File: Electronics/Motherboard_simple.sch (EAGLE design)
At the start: 23 parts

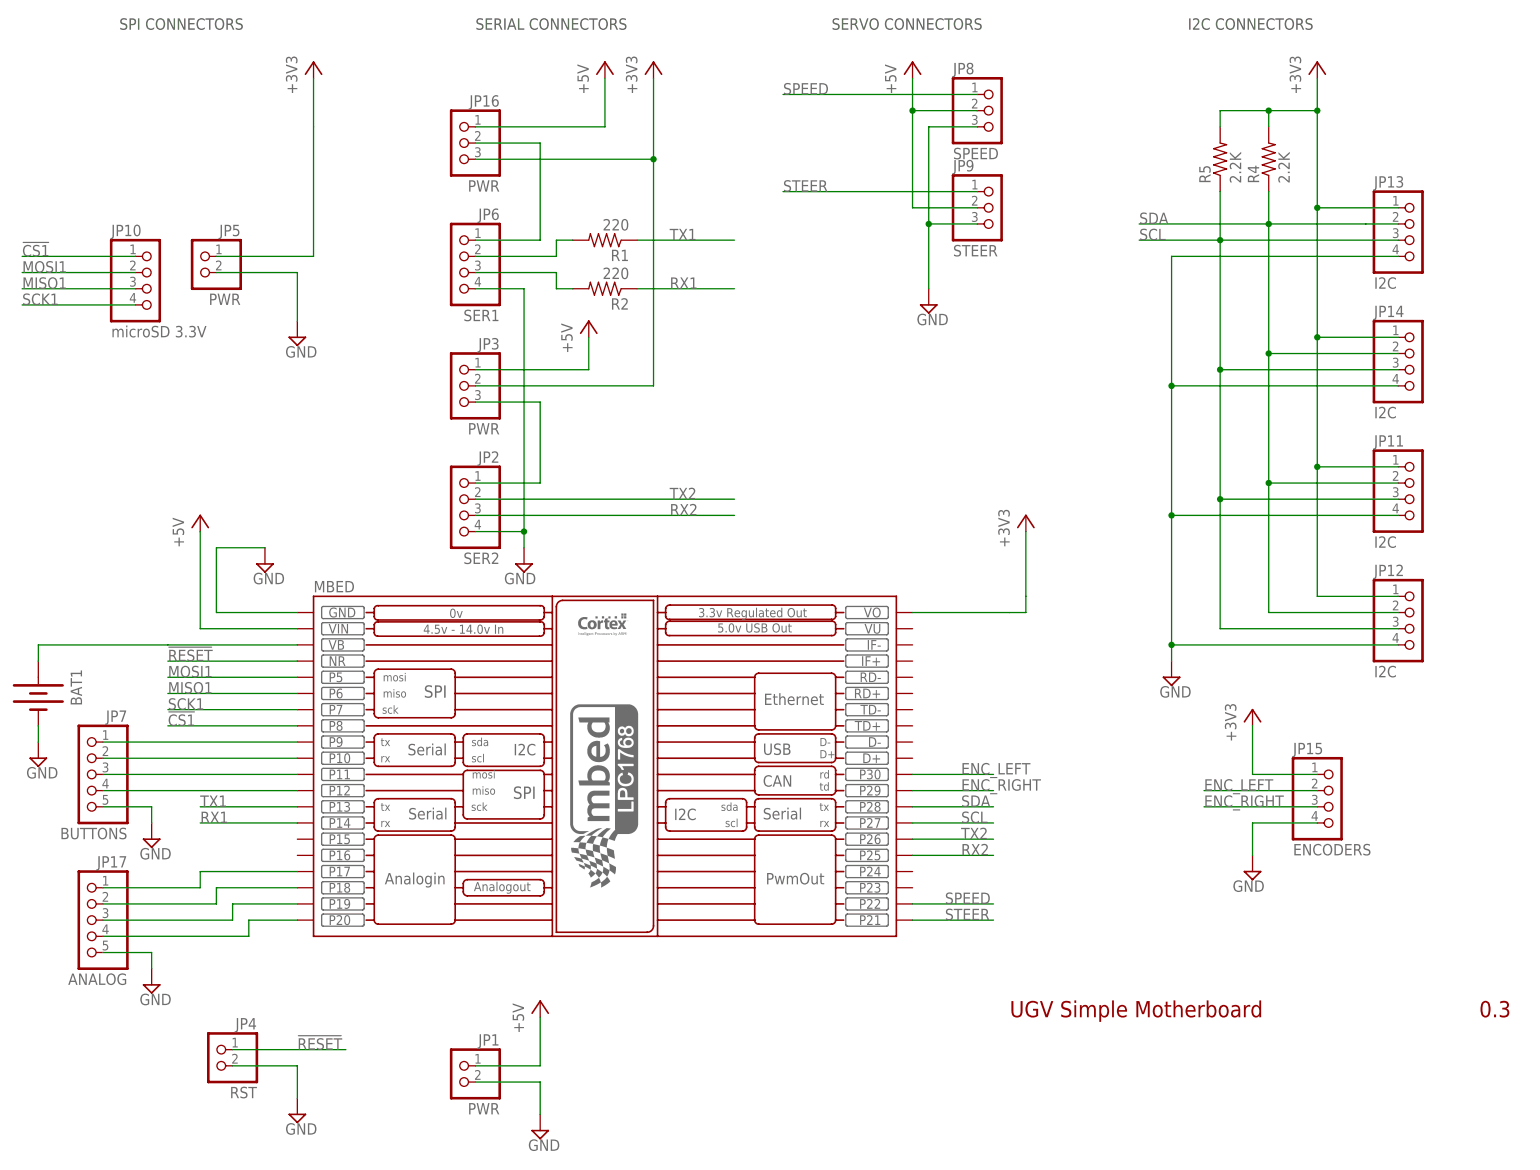
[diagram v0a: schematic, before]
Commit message: Initial Revision for microSD breakout, revised microsd pin header for motherboard, other minor tweaks to motherboard.
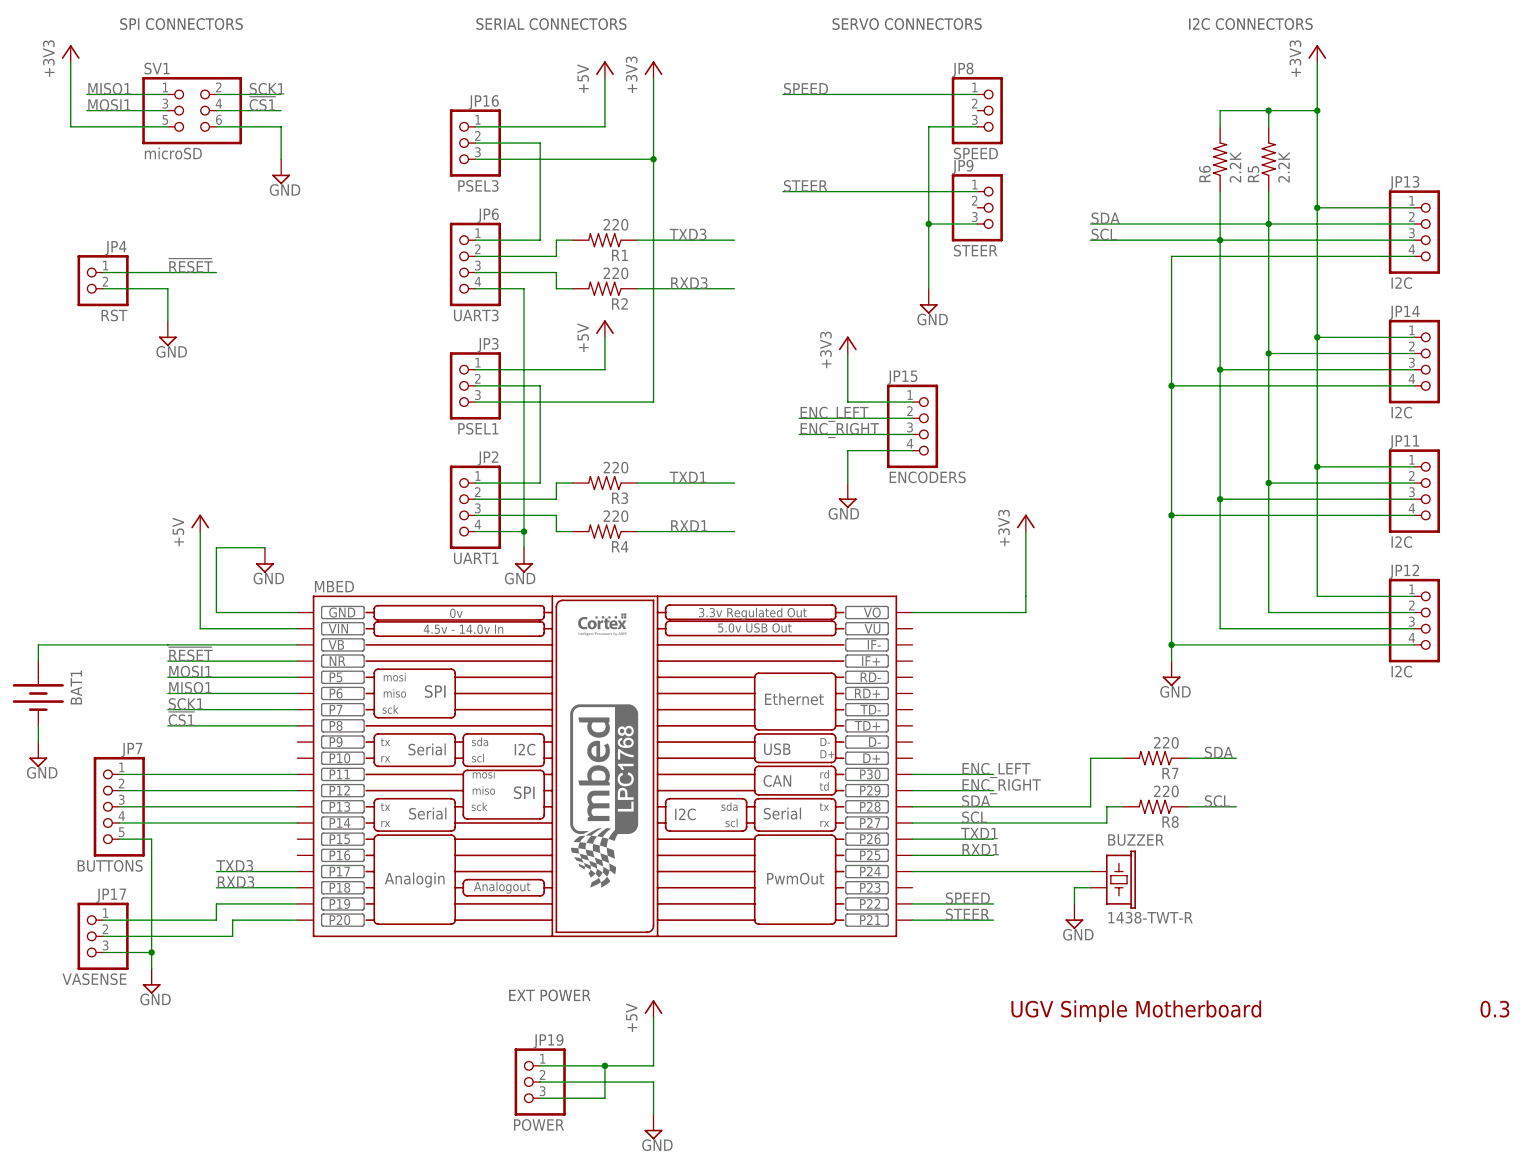
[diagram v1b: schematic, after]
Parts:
- removed JP1: PWR, pinhead-2:PINHD-1X02_2.54-90°-S
- removed JP10: microSD 3.3V, pinhead-2:PINHD-1X04_2.54-S
- removed JP5: PWR, pinhead-2:PINHD-1X02_2.54-S
- added BUZZER: 1438-TWT-R, mes_buzzers:BUZZER-AT-1438-TWT-R
- added JP19: POWER, pinhead-2:PINHD-1X03_2.54-S
- added R3, R7, R8: 220, rcl:R-US_R0805
- added R6: 2.2K, rcl:R-US_0204/5
- added SV1: microSD, pinhead-2:PINHD-2X03_2.54
- BAT1: MF (none) -> KEYSTONE ELECTR; MPN (none) -> 3001; OC_NEWARK (none) -> 66F5623; PARTNO (none) -> 3001
- JP11, JP12, JP13, JP14, JP15, JP4, JP7, JP8, JP9, R5: OC_NEWARK (none) -> unknown
- JP16: value PWR -> PSEL3; MPN (none) -> BF020-03-A-B-0600-0300-N-G; OC_NEWARK (none) -> 67R7706
- JP17: value ANALOG -> VASENSE; device pinhead-2:PINHD-1X05_2.54-S -> pinhead-2:PINHD-1X03_2.54-S; OC_NEWARK (none) -> unknown
- JP2: value SER2 -> UART1; OC_NEWARK (none) -> unknown
- JP3: value PWR -> PSEL1; MPN (none) -> BF020-03-A-B-0600-0300-N-G; OC_NEWARK (none) -> 67R7706
- JP6: value SER1 -> UART3; OC_NEWARK (none) -> unknown
- MBED: MPN (none) -> 2212S-20SG-85; OC_NEWARK (none) -> 08N6778
- R1, R2: device rcl:R-US_R0603 -> rcl:R-US_R0805; MPN (none) -> WCR0805-220RFI; OC_NEWARK (none) -> 98K2621
- R4: value 2.2K -> 220; device rcl:R-US_0204/5 -> rcl:R-US_R0805; MPN (none) -> WCR0805-220RFI; OC_NEWARK (none) -> 98K2621
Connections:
- removed net RX1: MBED.P14, R2.1
- removed net RX2: JP2.3, MBED.P25
- removed net TX1: MBED.P13, R1.1
- removed net TX2: JP2.2, MBED.P26
- new net N$12: BUZZER.1, MBED.P24
- new net N$13: MBED.P28, R7.2
- new net N$14: MBED.P27, R8.2
- new net RXD1: MBED.P25, R4.1
- new net RXD3: MBED.P18, R2.1
- new net TXD1: MBED.P26, R3.1
- new net TXD3: MBED.P17, R1.1
- net !CS1: now also SV1.4; no longer JP10.1
- net +3V3: now also JP3.3, R6.2, SV1.5; no longer JP3.2, JP5.1, R4.2
- net +5V: now also JP19.1, JP19.3; no longer JP1.1, JP8.2, JP9.2
- net AMP: now also JP17.2; no longer JP17.4
- net GND: now also BUZZER.2, JP17.3, JP19.2, SV1.6; no longer JP1.2, JP17.5, JP5.2
- net MISO1: now also SV1.1; no longer JP10.3
- net MOSI1: now also SV1.3; no longer JP10.2
- net N$10: now also JP2.3, R4.2; no longer JP17.1, MBED.P17
- net N$11: now also JP3.2; no longer JP3.3
- net N$4: now also MBED.P11; no longer MBED.P9
- net N$5: now also MBED.P12; no longer MBED.P10
- net N$6: now also JP17.1; no longer JP17.3
- net N$7: now also MBED.P13; no longer MBED.P11
- net N$8: now also MBED.P14; no longer MBED.P12
- net N$9: now also JP2.2, R3.2; no longer JP17.2, MBED.P18
- net SCK1: now also SV1.2; no longer JP10.4
- net SCL: now also R6.1, R8.1; no longer MBED.P27, R5.1
- net SDA: now also R5.1, R7.1; no longer MBED.P28, R4.1
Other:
- note added: "EXT POWER"
- moved on the sheet: JP11, JP12, JP13, JP14, JP15, JP4, JP7, R4, R5

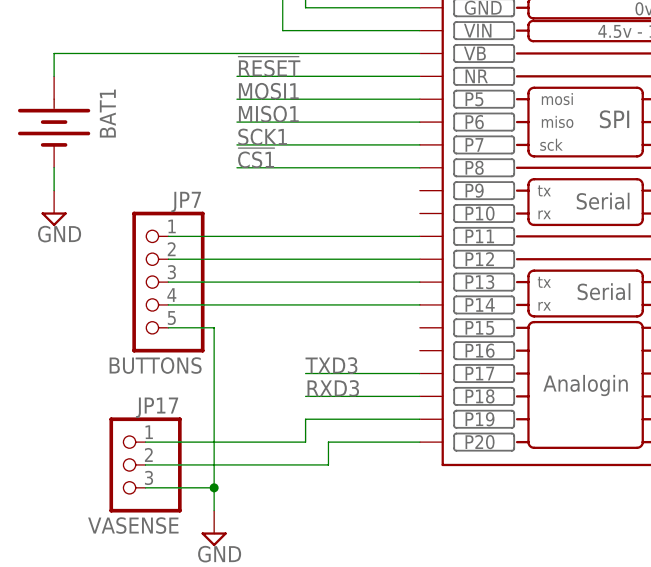
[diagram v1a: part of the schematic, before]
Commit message: Tweaks to make room for SPI2
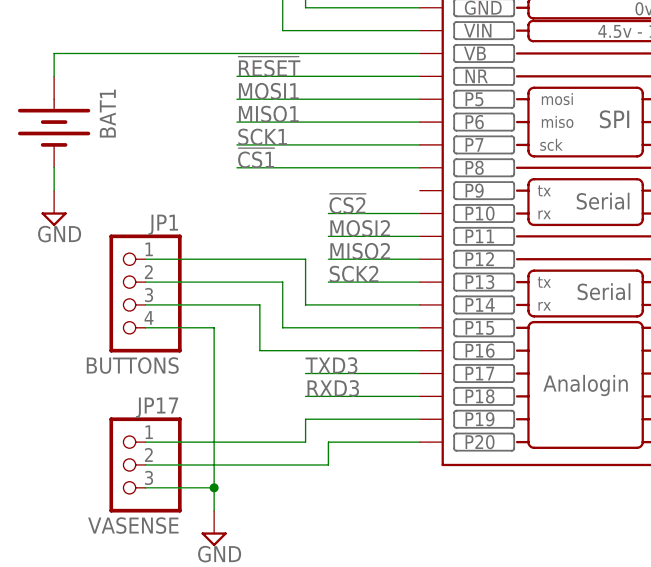
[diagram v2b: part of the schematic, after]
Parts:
- removed JP7: BUTTONS, pinhead-2:PINHD-1X05_2.54-S
- added JP1: BUTTONS, pinhead-2:PINHD-1X04_2.54-S
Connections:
- removed net N$4: JP7.1, MBED.P11
- new net !CS2: MBED.P10
- new net MISO2: MBED.P12
- new net MOSI2: MBED.P11
- new net SCK2: MBED.P13
- net GND: now also JP1.4; no longer JP7.5
- net N$5: now also JP1.1, MBED.P14; no longer JP7.2, MBED.P12
- net N$7: now also JP1.2, MBED.P15; no longer JP7.3, MBED.P13
- net N$8: now also JP1.3, MBED.P16; no longer JP7.4, MBED.P14

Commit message: Minor updates and tweaks
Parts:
- removed JP16: PSEL3, pinhead-2:PINHD-1X03_2.54-S
- removed JP3: PSEL1, pinhead-2:PINHD-1X03_2.54-S
- added JP10: UART2, pinhead-2:PINHD-1X04_2.54-S
- added JP5: I2C, pinhead-2:PINHD-1X04_2.54-S
- added JP7: PPS, pinhead-2:PINHD-1X01_2.54-S
- added R10, R9: 220, rcl:R-US_R0805
- BAT1: device SparkFun:BATTERY12PTH -> SparkFun:BATTERY12MM
- JP1: device pinhead-2:PINHD-1X04_2.54-S -> pinhead-2:PINHD-2X02_2.54; OC_NEWARK unknown -> (none)
- JP17: value VASENSE -> VA
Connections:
- removed net !CS2: MBED.P10
- removed net MISO2: MBED.P12
- removed net MOSI2: MBED.P11
- removed net N$11: JP2.1, JP3.2
- removed net N$3: JP16.2, JP6.1
- removed net SCK2: MBED.P13
- new net N$16: JP10.2, R9.2
- new net N$17: JP10.3, R10.2
- new net PPS: JP7.1, MBED.P23
- new net RXD2: MBED.P10, R10.1
- new net TXD2: MBED.P9, R9.1
- net +3V3: now also JP10.1, JP2.1, JP5.1, JP6.1; no longer JP16.3, JP3.3
- net +5V: no longer JP16.1, JP3.1
- net GND: now also JP1.1, JP10.4, JP5.4; no longer JP1.4
- net N$5: now also JP1.2; no longer JP1.1
- net N$7: now also JP1.4; no longer JP1.2
- net SCL: now also JP5.3
- net SDA: now also JP5.2
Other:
- moved on the sheet: JP1, JP11, JP12, JP13, JP14, JP17, JP2, JP4, JP6, R1, R2, R3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

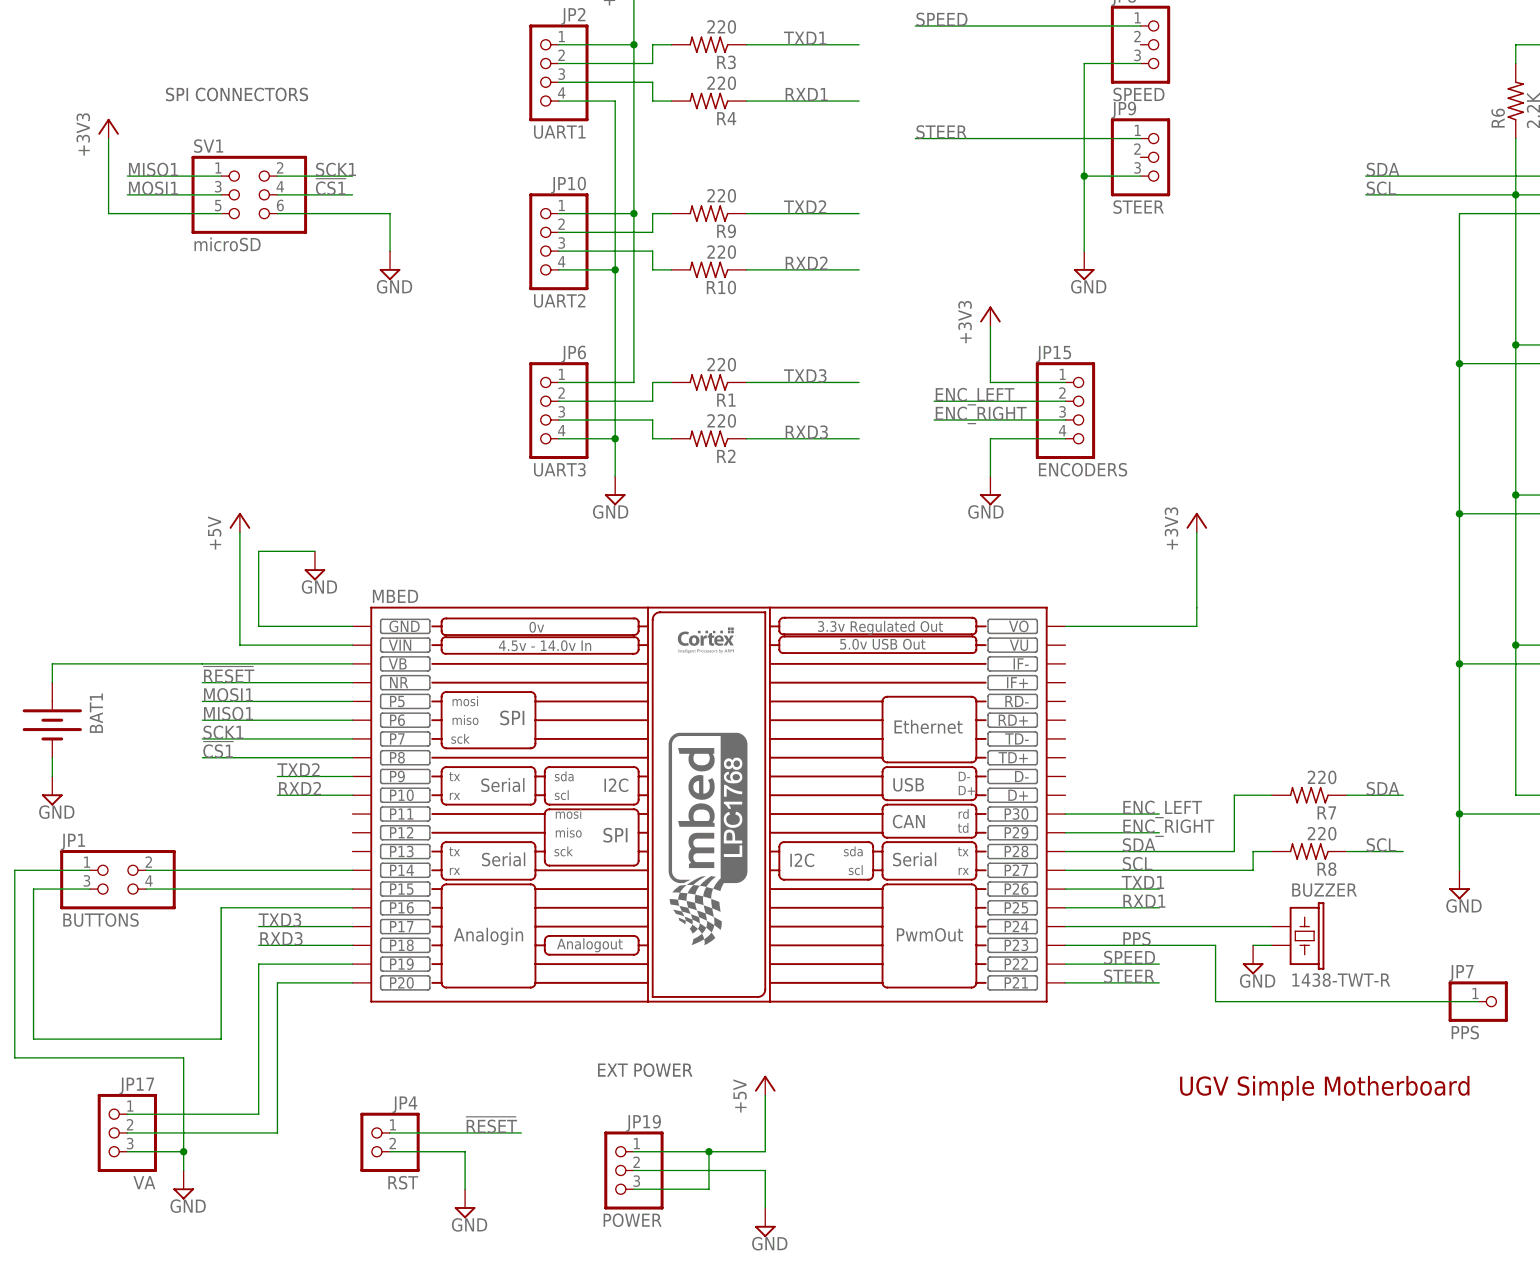
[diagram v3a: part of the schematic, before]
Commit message: Removed battery, added microSD, more room now, yay.
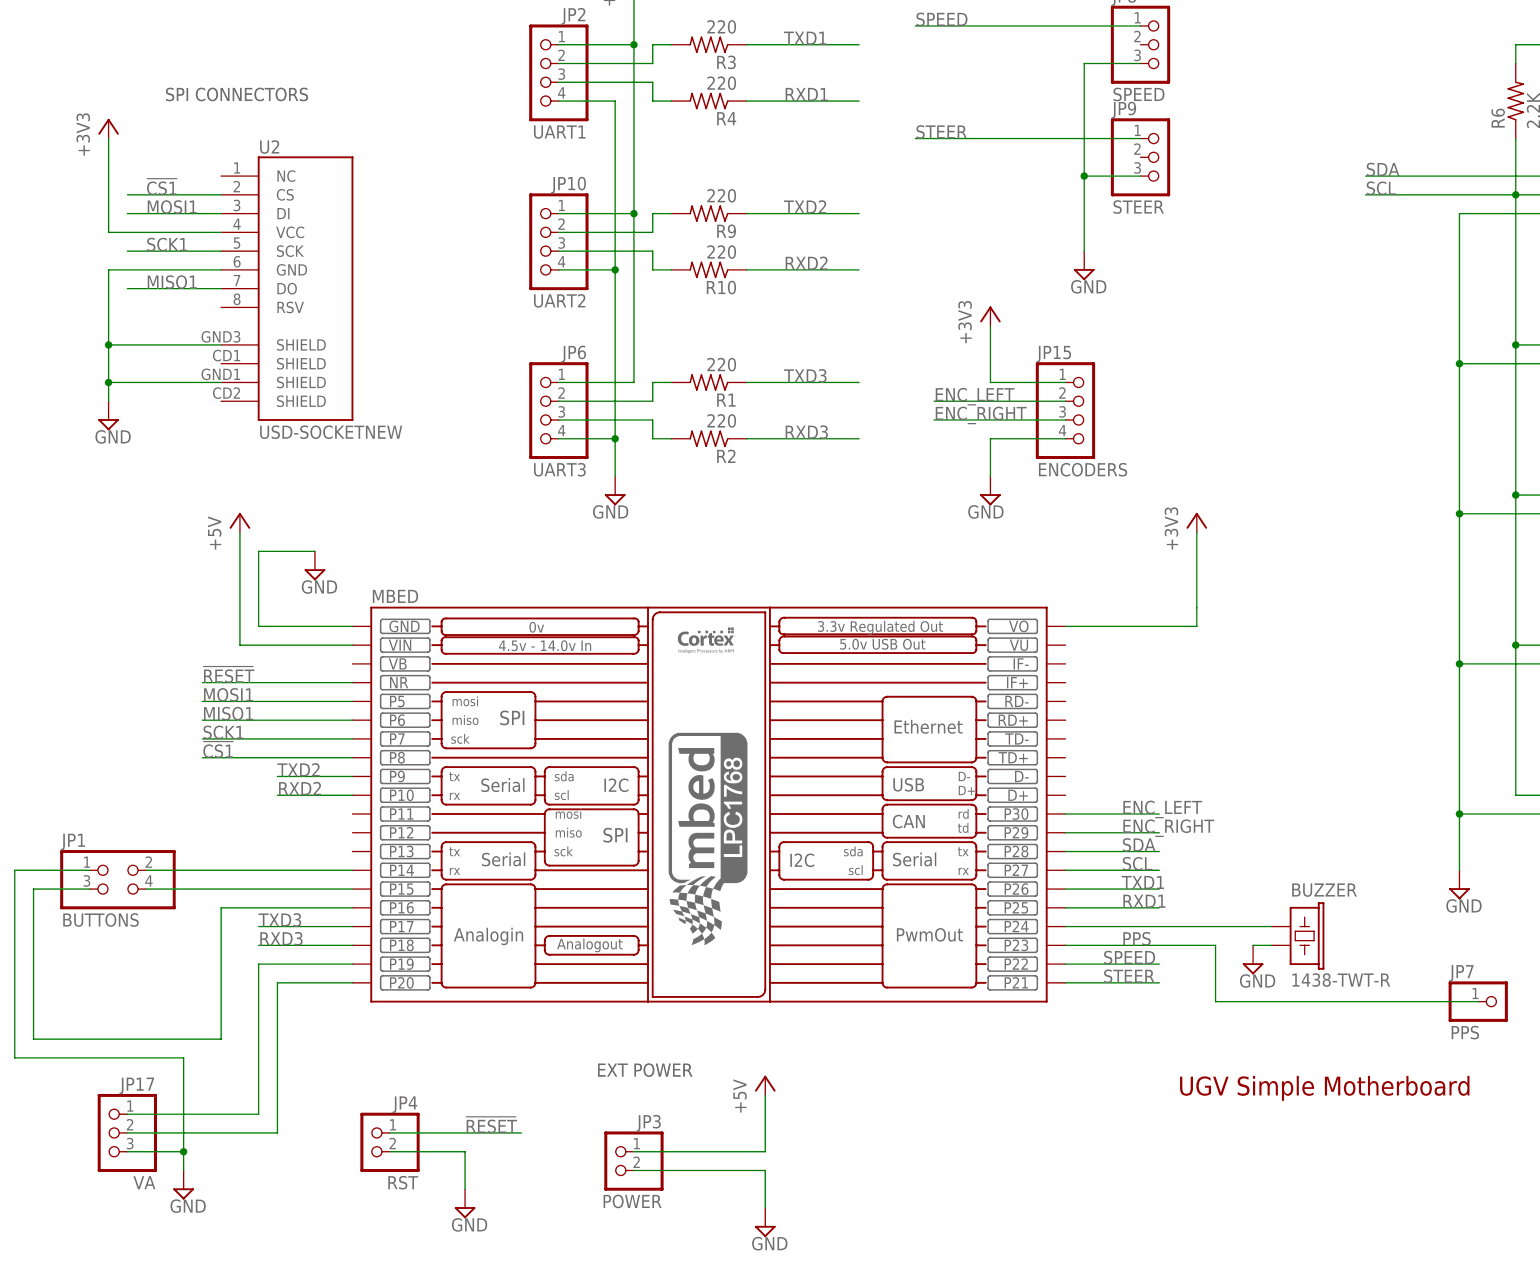
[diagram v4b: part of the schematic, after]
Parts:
- removed BAT1: (no value), SparkFun:BATTERY12MM
- removed JP19: POWER, pinhead-2:PINHD-1X03_2.54-S
- removed R7, R8: 220, rcl:R-US_R0805
- removed SV1: microSD, pinhead-2:PINHD-2X03_2.54
- added JP3: POWER, pinhead-2:PINHD-1X02_2.54-90°-S
- added U2: USD-SOCKETNEW, SparkFun:USD-SOCKETNEW
- R1, R10, R2, R3, R4, R9: device rcl:R-US_R0805 -> rcl:R-US_0204/5
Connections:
- removed net N$13: MBED.P28, R7.2
- removed net N$14: MBED.P27, R8.2
- removed net VB: BAT1.+, MBED.VB
- net !CS1: now also U2.CS; no longer SV1.4
- net +3V3: now also U2.VCC; no longer SV1.5
- net +5V: now also JP3.1; no longer JP19.1, JP19.3
- net GND: now also JP3.2, U2.GND, U2.SHIELD@1, U2.SHIELD@3; no longer BAT1.-, JP19.2, SV1.6
- net MISO1: now also U2.DO; no longer SV1.1
- net MOSI1: now also U2.DI; no longer SV1.3
- net SCK1: now also U2.SCK; no longer SV1.2
- net SCL: now also MBED.P27; no longer R8.1
- net SDA: now also MBED.P28; no longer R7.1
